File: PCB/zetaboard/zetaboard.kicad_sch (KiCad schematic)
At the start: 175 parts, among them SW1 RotaryEncoder_Switch, SW2 RotaryEncoder_Switch, U1 Raspberry_Pi_Pico_2W, U2 TM1637_Module

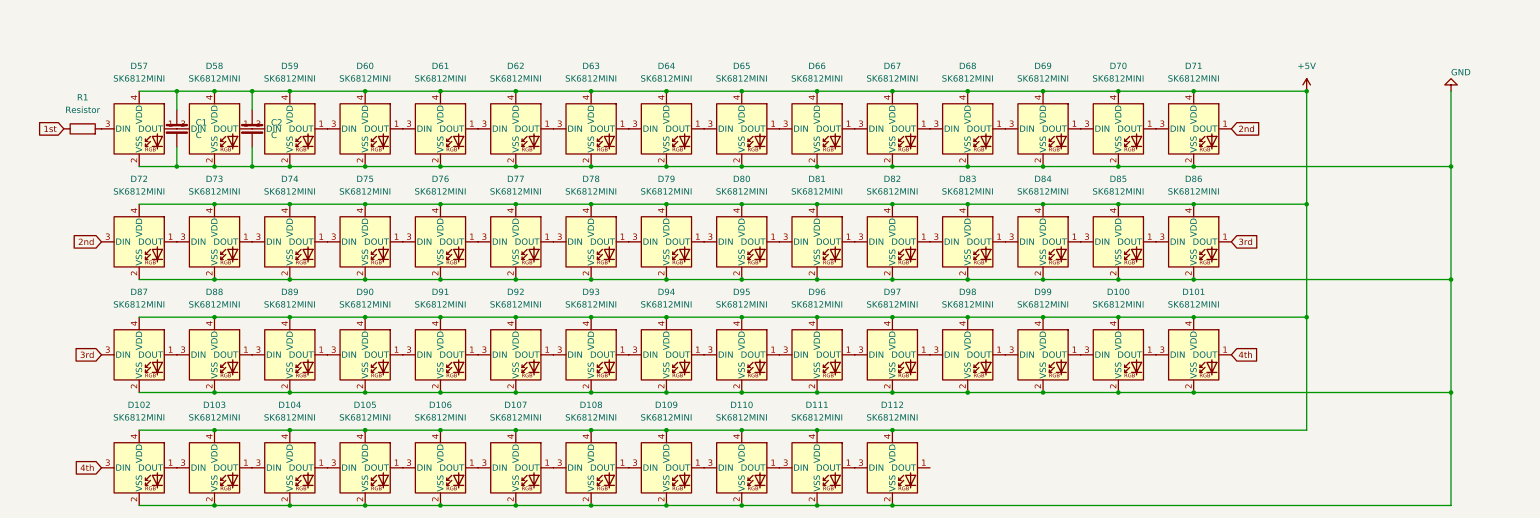
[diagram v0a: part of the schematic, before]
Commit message: Schematic finished and PCB started.
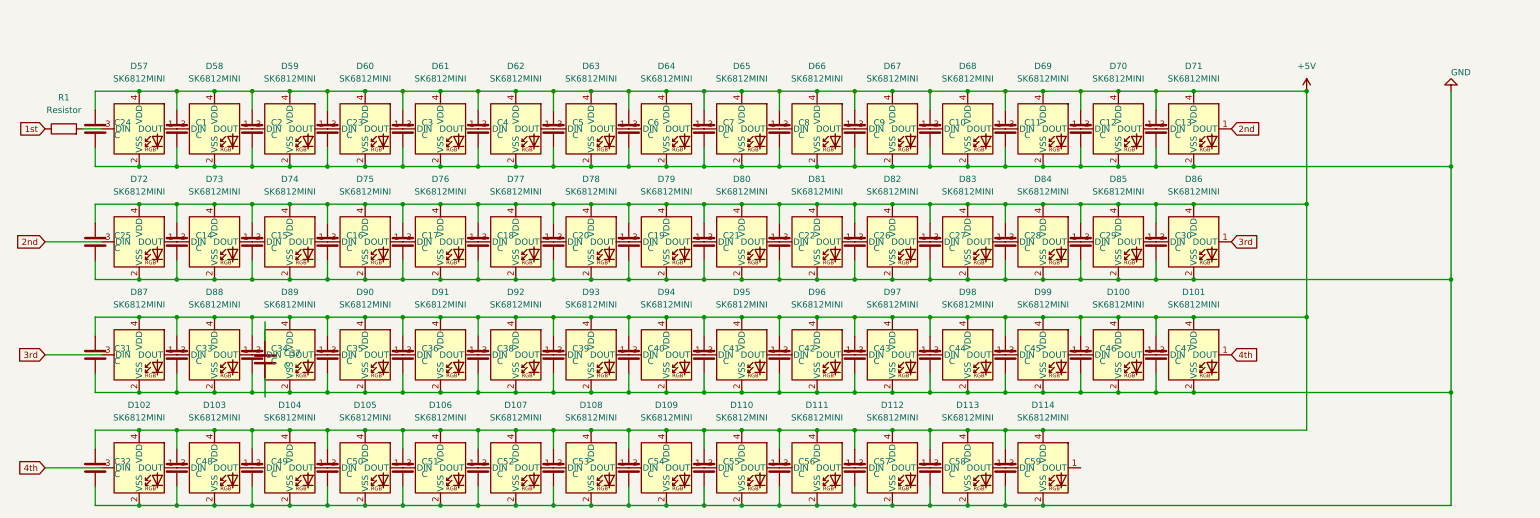
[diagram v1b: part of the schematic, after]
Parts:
- added C10, C11, C12, C13, C14, C15, C16, C17, C18, C19, C20, C21, C22, C23, C24, C25, C26, C27, C28, C29, C3, C30, C31, C32, C33, C34, C35, C36, C37, C38, C39, C4, C40, C41, C42, C43, C44, C45, C46, C47, C48, C49, C5, C50, C51, C52, C53, C54, C55, C56, C57, C58, C59, C6, C7, C8, C9: C, Capacitor_SMD:C_0805_2012Metric, symbol Device:C
- added D113, D114: SK6812MINI, LED_SMD:LED_SK6812MINI_PLCC4_3.5x3.5mm_P1.75mm, symbol LED:SK6812MINI
- C1, C2: footprint (none) -> Capacitor_SMD:C_0805_2012Metric
- R1: footprint (none) -> Resistor_SMD:R_0805_2012Metric
- S1, S10, S13, S14, S15, S16, S17, S18, S19, S2, S20, S21, S22, S26, S27, S28, S29, S3, S30, S31, S32, S33, S34, S35, S38, S39, S4, S40, S41, S42, S43, S44, S45, S46, S47, S48, S49, S5, S50, S51, S52, S54, S55, S56, S6, S7, S8, S9: footprint (none) -> ScottoKeebs_Hotswap:Hotswap_MX_1.00u
- S11: footprint (none) -> ScottoKeebs_Hotswap:Hotswap_MX_2.00u
- S12: footprint (none) -> ScottoKeebs_Hotswap:Hotswap_MX_1.50u
- S23, S24: footprint (none) -> ScottoKeebs_Hotswap:Hotswap_MX_1.25u
- S36, S37: footprint (none) -> ScottoKeebs_Hotswap:Hotswap_MX_2.25u
- S53: footprint (none) -> ScottoKeebs_Hotswap:Hotswap_MX_6.25u
- U2: footprint (none) -> TM137:TM1637 Display Module
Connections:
- net +5V: now also C10.1, C11.1, C12.1, C13.1, C14.1, C15.1, C16.1, C17.1, C18.1, C19.1, C20.1, C21.1, C22.1, C23.1, C24.1, C25.1, C26.1, C27.1, C28.1, C29.1, C3.1, C30.1, C31.1, C32.1, C33.1, C34.1, C35.1, C36.1, C38.1, C39.1, C4.1, C40.1, C41.1, C42.1, C43.1, C44.1, C45.1, C46.1, C47.1, C48.1, C49.1, C5.1, C50.1, C51.1, C52.1, C53.1, C54.1, C55.1, C56.1, C57.1, C58.1, C59.1, C6.1, C7.1, C8.1, C9.1, D113.4 (VDD), D114.4 (VDD)
- net GND: now also C10.2, C11.2, C12.2, C13.2, C14.2, C15.2, C16.2, C17.2, C18.2, C19.2, C20.2, C21.2, C22.2, C23.2, C24.2, C25.2, C26.2, C27.2, C28.2, C29.2, C3.2, C30.2, C31.2, C32.2, C33.2, C34.2, C35.2, C36.2, C38.2, C39.2, C4.2, C40.2, C41.2, C42.2, C43.2, C44.2, C45.2, C46.2, C47.2, C48.2, C49.2, C5.2, C50.2, C51.2, C52.2, C53.2, C54.2, C55.2, C56.2, C57.2, C58.2, C59.2, C6.2, C7.2, C8.2, C9.2, D113.2 (VSS), D114.2 (VSS)
- net at D112.1 (DOUT): now also D113.3 (DIN)
- new net: D113.1 (DOUT), D114.3 (DIN)
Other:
- moved on the sheet: R1

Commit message: Save commit just in case I mess something up with removing the capacitors
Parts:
- removed C58, C59: C, Capacitor_SMD:C_0805_2012Metric, symbol Device:C
- removed D113, D114: SK6812MINI, LED_SMD:LED_SK6812MINI_PLCC4_3.5x3.5mm_P1.75mm, symbol LED:SK6812MINI

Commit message: Still on the PCB
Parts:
- removed C1, C10, C11, C12, C13, C14, C15, C16, C17, C18, C19, C2, C20, C21, C22, C23, C24, C25, C26, C27, C28, C29, C3, C30, C31, C32, C33, C34, C35, C36, C37, C38, C39, C4, C40, C41, C42, C43, C44, C45, C46, C47, C48, C49, C5, C50, C51, C52, C53, C54, C55, C56, C57, C6, C7, C8, C9: C, Capacitor_SMD:C_0805_2012Metric, symbol Device:C

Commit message: (Basically) finished PCB and started work on plate
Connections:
- net 1st: now also U1.1 (GPIO0); no longer U1.34 (GPIO28_ADC2)
- net CLK: now also U1.32 (GPIO27_ADC1); no longer U1.1 (GPIO0)
- net Col 0: now also S25.1, U1.2 (GPIO1); no longer U1.4 (GPIO2)
- net Col 1: now also S26.1, U1.4 (GPIO2); no longer S25.1, U1.5 (GPIO3)
- net Col 10: now also S35.1, S55.1, U1.15 (GPIO11); no longer S34.1, U1.16 (GPIO12)
- net Col 11: now also S36.1, S56.1, U1.16 (GPIO12); no longer S35.1, U1.17 (GPIO13)
- net Col 12: now also SW2.S2, U1.17 (GPIO13); no longer S36.1, U1.31 (GPIO26_ADC0)
- net Col 2: now also S27.1, U1.5 (GPIO3); no longer S26.1, U1.6 (GPIO4)
- net Col 3: now also S28.1, U1.6 (GPIO4); no longer S27.1, U1.7 (GPIO5)
- net Col 4: now also S29.1, U1.7 (GPIO5); no longer S28.1, U1.9 (GPIO6)
- net Col 5: now also S30.1, U1.9 (GPIO6); no longer S29.1, S54.1, U1.10 (GPIO7)
- net Col 6: now also S31.1, U1.10 (GPIO7); no longer S30.1, S55.1, U1.11 (GPIO8)
- net Col 7: now also S32.1, U1.11 (GPIO8); no longer S31.1, S56.1, U1.12 (GPIO9)
- net Col 8: now also S33.1, U1.12 (GPIO9); no longer S32.1, SW2.S2, U1.14 (GPIO10)
- net Col 9: now also S34.1, S54.1, U1.14 (GPIO10); no longer S33.1, U1.15 (GPIO11)
- net DIO: now also U1.31 (GPIO26_ADC0); no longer U1.2 (GPIO1)
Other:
- moved on the sheet: D25, D26, D27, D28, D29, D30, D31, D32, D33, D34, D35, D36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
